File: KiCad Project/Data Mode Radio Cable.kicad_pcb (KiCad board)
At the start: 2 copper layers, 40 x 37 mm, 15 parts, among them J1 TRRS, J2 2.5mm, J3 3.5mm, J4 RS232, SW1 PTT_LOCK, T1 600R, U1 PC817

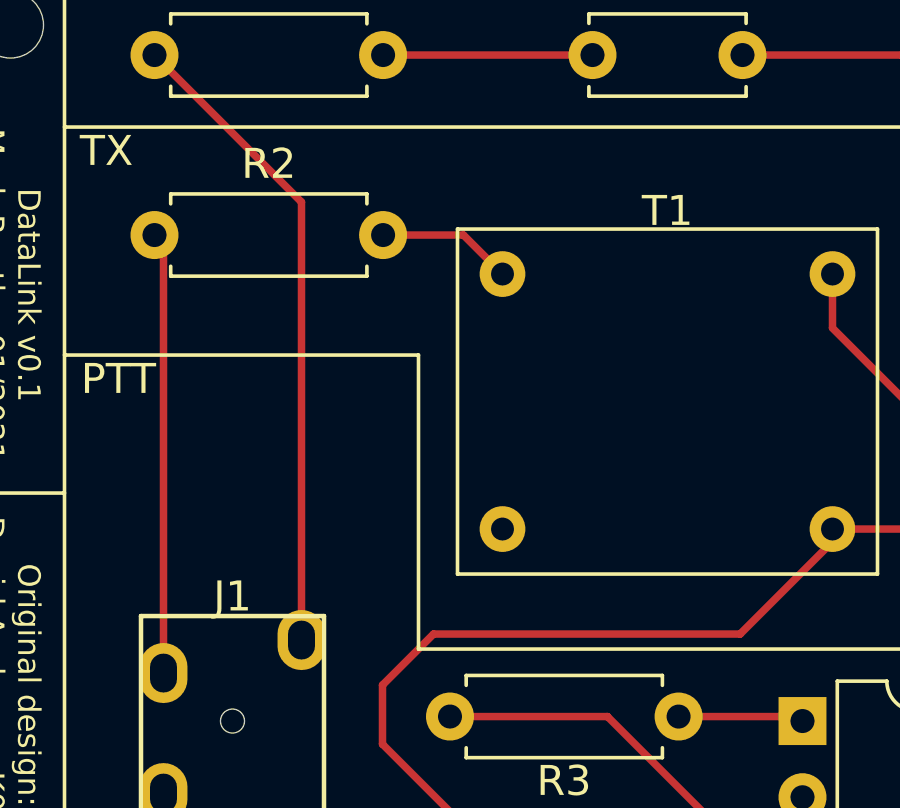
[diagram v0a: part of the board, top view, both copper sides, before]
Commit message: Add files via upload
Replaced project files with ones pointing to new per-project footprints
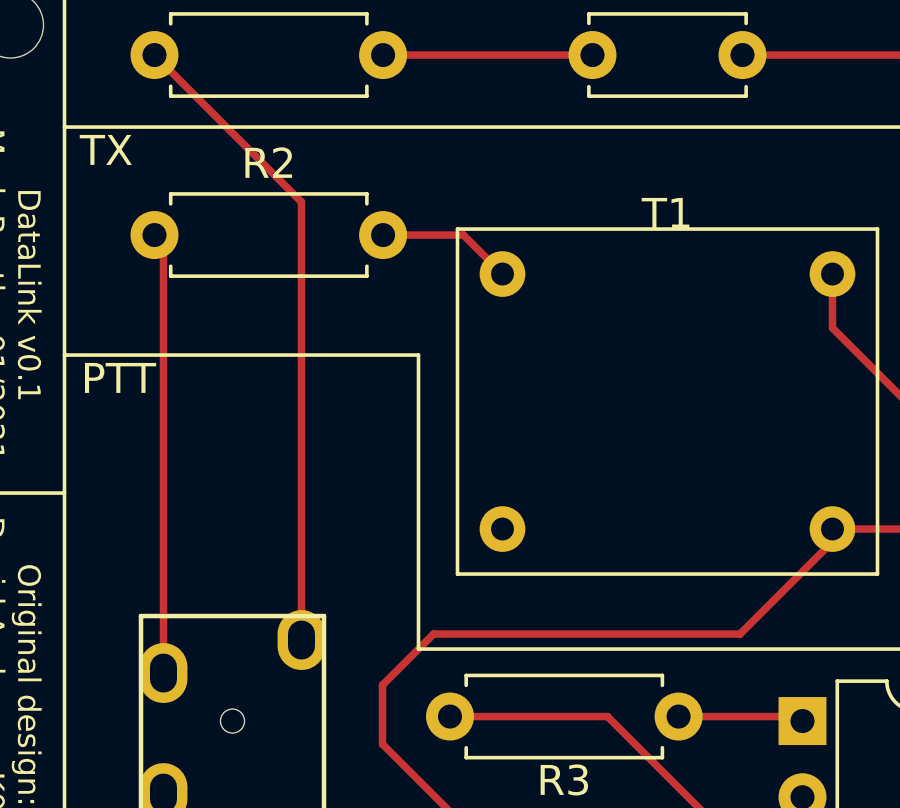
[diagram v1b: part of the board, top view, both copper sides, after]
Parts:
- J1: footprint Keebio-Parts:TRRS-PJ-320A -> Library:TRRS-PJ-320A
- SW1: footprint Custom_Footprints:SPDT_Right_Angled_Switch -> Library:SPDT_Right_Angled_Switch
- T1: footprint Custom_Footprints:1-1_Audio_Transformer_600_ohm -> Library:1-1_Audio_Transformer_600_ohm
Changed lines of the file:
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@@
     (pad "" np_thru_hole circle locked (at 0 0) (size 2.2 2.2) (drill 2.2) (layers *.Cu *.Mask))
   )
-  (footprint "Keebio-Parts:TRRS-PJ-320A" (layer "F.Cu")
+  (footprint "Library:TRRS-PJ-320A" (layer "F.Cu")
     (at 58.6 79 180)
     (property "Sheetfile" "Data Mode Radio Cable.kicad_sch")
     (property "Sheetname" "")
     (attr through_hole)
-    (fp_text reference "J1" (at 0 12.75 180) (layer "F.SilkS")
+    (fp_text reference "J1" (at 0 14.2 180) (layer "Dwgs.User")
       (effects (font (size 1 1) (thickness 0.15)))
     )
@@
       (effects (font (size 1 1) (thickness 0.15)))
     )
+    (fp_text user "Tip" (at 0 10 180) (layer "F.Fab")
+      (effects (font (size 0.7 0.7) (thickness 0.1)))
+    )
     (fp_text user "Ring2" (at 0 3.25 180) (layer "F.Fab")
       (effects (font (size 0.7 0.7) (thickness 0.1)))
     )
-    (fp_text user "Tip" (at 0 10 180) (layer "F.Fab")
+    (fp_text user "Sleeve" (at 0.25 11.4 180) (layer "F.Fab")
       (effects (font (size 0.7 0.7) (thickness 0.1)))
     )
@@
       (effects (font (size 0.7 0.7) (thickness 0.1)))
     )
-    (fp_text user "Sleeve" (at 0.25 11.4 180) (layer "F.Fab")
-      (effects (font (size 0.7 0.7) (thickness 0.1)))
-    )
+    (fp_line (start -2.8 0) (end -2.8 -2) (layer "F.SilkS") (width 0.15))
+    (fp_line (start 3.05 12.1) (end -3.05 12.1) (layer "F.SilkS") (width 0.15))
+    (fp_line (start 3.05 0) (end 3.05 12.1) (layer "F.SilkS") (width 0.15))
+    (fp_line (start 3.05 0) (end -3.05 0) (layer "F.SilkS") (width 0.15))
+    (fp_line (start 2.8 -2) (end -2.8 -2) (layer "F.SilkS") (width 0.15))
+    (fp_line (start 2.8 0) (end 2.8 -2) (layer "F.SilkS") (width 0.15))
     (fp_line (start -3.05 0) (end -3.05 12.1) (layer "F.SilkS") (width 0.15))
-    (fp_line (start 2.8 -2) (end -2.8 -2) (layer "F.SilkS") (width 0.15))
-    (fp_line (start 3.05 0) (end -3.05 0) (layer "F.SilkS") (width 0.15))
-    (fp_line (start 3.05 12.1) (end -3.05 12.1) (layer "F.SilkS") (width 0.15))
-    (fp_line (start -2.8 0) (end -2.8 -2) (layer "F.SilkS") (width 0.15))
-    (fp_line (start 2.8 0) (end 2.8 -2) (layer "F.SilkS") (width 0.15))
-    (fp_line (start 3.05 0) (end 3.05 12.1) (layer "F.SilkS") (width 0.15))
-    (pad "" np_thru_hole circle locked (at 0 8.6 180) (size 0.8 0.8) (drill 0.8) (layers *.Cu *.Mask))
-    (pad "" np_thru_hole circle locked (at 0 1.6 180) (size 0.8 0.8) (drill 0.8) (layers *.Cu *.Mask))
-    (pad "R1" thru_hole oval locked (at 2.3 6.2 180) (size 1.6 2) (drill oval 0.9 1.3) (layers *.Cu *.Mask)
+    (pad "" np_thru_hole circle (at 0 8.6 180) (size 0.8 0.8) (drill 0.8) (layers *.Cu *.Mask))
+    (pad "" np_thru_hole circle (at 0 1.6 180) (size 0.8 0.8) (drill 0.8) (layers *.Cu *.Mask))
+    (pad "R1" thru_hole oval (at 2.3 6.2 180) (size 1.6 2) (drill oval 0.9 1.3) (layers *.Cu *.Mask)
       (net 12 "unconnected-(J1-PadR1)") (pintype "passive+no_connect"))
-    (pad "R2" thru_hole oval locked (at 2.3 3.2 180) (size 1.6 2) (drill oval 0.9 1.3) (layers *.Cu *.Mask)
+    (pad "R2" thru_hole oval (at 2.3 3.2 180) (size 1.6 2) (drill oval 0.9 1.3) (layers *.Cu *.Mask)
       (net 3 "GND") (pintype "passive"))
-    (pad "S" thru_hole oval locked (at -2.3 11.3 180) (size 1.6 2) (drill oval 0.9 1.3) (layers *.Cu *.Mask)
+    (pad "S" thru_hole oval (at -2.3 11.3 180) (size 1.6 2) (drill oval 0.9 1.3) (layers *.Cu *.Mask)
       (net 6 "Net-(J1-PadS)") (pintype "passive"))
-    (pad "T" thru_hole oval locked (at 2.3 10.2 180) (size 1.6 2) (drill oval 0.9 1.3) (layers *.Cu *.Mask)
+    (pad "T" thru_hole oval (at 2.3 10.2 180) (size 1.6 2) (drill oval 0.9 1.3) (layers *.Cu *.Mask)
       (net 7 "Net-(J1-PadT)") (pintype "passive"))
-    (model "${KISYS3DMOD}/Custom.3dshapes/PJ-320A.step"
+    (model "${KIPRJMOD}/3D Models/PJ-320A.step"
       (offset (xyz 0 -1 0))
       (scale (xyz 1 1 1))
@@
     )
   )
-  (footprint "Custom_Footprints:1-1_Audio_Transformer_600_ohm" (layer "F.Cu")
+  (footprint "Library:1-1_Audio_Transformer_600_ohm" (layer "F.Cu")
     (at 73.1 67)
     (property "Sheetfile" "Data Mode Radio Cable.kicad_sch")
     (property "Sheetname" "")
     (attr through_hole)
-    (fp_text reference "T1" (at 0 -13.6) (layer "F.SilkS")
+    (fp_text reference "T1" (at 0 -13.5) (layer "F.SilkS")
       (effects (font (size 1 1) (thickness 0.15)))
     )
@@
       (effects (font (size 1 1) (thickness 0.15)))
     )
+    (fp_line (start -7 -1.5) (end 7 -1.5) (layer "F.SilkS") (width 0.12))
+    (fp_line (start 7 -13) (end -7 -13) (layer "F.SilkS") (width 0.12))
     (fp_line (start -7 -13) (end -7 -1.5) (layer "F.SilkS") (width 0.12))
     (fp_line (start 7 -1.5) (end 7 -13) (layer "F.SilkS") (width 0.12))
-    (fp_line (start 7 -13) (end -7 -13) (layer "F.SilkS") (width 0.12))
-    (fp_line (start -7 -1.5) (end 7 -1.5) (layer "F.SilkS") (width 0.12))
-    (pad "1" thru_hole circle locked (at -5.5 -11.5) (size 1.524 1.524) (drill 0.762) (layers *.Cu *.Mask)
+    (pad "1" thru_hole circle (at -5.5 -11.5) (size 1.524 1.524) (drill 0.762) (layers *.Cu *.Mask)
       (net 8 "Net-(R2-Pad2)") (pinfunction "AA") (pintype "passive"))
-    (pad "2" thru_hole circle locked (at -5.5 -3) (size 1.524 1.524) (drill 0.762) (layers *.Cu *.Mask)
+    (pad "2" thru_hole circle (at -5.5 -3) (size 1.524 1.524) (drill 0.762) (layers *.Cu *.Mask)
       (net 3 "GND") (pinfunction "AB") (pintype "passive"))
-    (pad "3" thru_hole circle locked (at 5.5 -3) (size 1.524 1.524) (drill 0.762) (layers *.Cu *.Mask)
+    (pad "3" thru_hole circle (at 5.5 -3) (size 1.524 1.524) (drill 0.762) (layers *.Cu *.Mask)
       (net 5 "Net-(J3-Pad2)") (pinfunction "SA") (pintype "passive"))
-    (pad "4" thru_hole circle locked (at 5.5 -11.5) (size 1.524 1.524) (drill 0.762) (layers *.Cu *.Mask)
+    (pad "4" thru_hole circle (at 5.5 -11.5) (size 1.524 1.524) (drill 0.762) (layers *.Cu *.Mask)
       (net 4 "Net-(J3-Pad1)") (pinfunction "SB") (pintype "passive"))
-    (model "${KISYS3DMOD}/Custom.3dshapes/4 pin audio transformer.wrl"
+    (model "${KIPRJMOD}/3D Models/4 pin audio transformer.wrl"
       (offset (xyz 0 0 0))
       (scale (xyz 1 1 1))
@@
     )
   )
-  (footprint "Custom_Footprints:SPDT_Right_Angled_Switch" (layer "F.Cu")
+  (footprint "Library:SPDT_Right_Angled_Switch" (layer "F.Cu")
     (at 68.55 77.9 180)
     (property "Sheetfile" "Data Mode Radio Cable.kicad_sch")
     (property "Sheetname" "")
     (attr through_hole)
-    (fp_text reference "SW1" (at -0.254 0.246) (layer "F.SilkS")
+    (fp_text reference "SW1" (at -0.254 0.246 180) (layer "F.SilkS")
       (effects (font (size 1 1) (thickness 0.15)))
     )
-    (fp_text value "PTT_LOCK" (at 0 3.81) (layer "F.Fab")
+    (fp_text value "PTT_LOCK" (at 0 3.81 180) (layer "F.Fab")
       (effects (font (size 1 1) (thickness 0.15)))
     )
     (fp_line (start 4.826 2.794) (end 4.826 -2.794) (layer "F.SilkS") (width 0.12))
-    (fp_line (start -4.826 2.794) (end 4.826 2.794) (layer "F.SilkS") (width 0.12))
-    (fp_line (start -4.826 -2.794) (end -4.826 2.794) (layer "F.SilkS") (width 0.12))
     (fp_line (start 4.826 -2.794) (end -4.826 -2.794) (layer "F.SilkS") (width 0.12))
     (fp_line (start -4.826 0.762) (end 4.826 0.762) (layer "F.SilkS") (width 0.12))
+    (fp_line (start -4.826 -2.794) (end -4.826 2.794) (layer "F.SilkS") (width 0.12))
+    (fp_line (start -4.826 2.794) (end 4.826 2.794) (layer "F.SilkS") (width 0.12))
+    (fp_line (start 5.08 3.048) (end -5.08 3.048) (layer "F.CrtYd") (width 0.05))
+    (fp_line (start 5.08 -3.048) (end 5.08 3.048) (layer "F.CrtYd") (width 0.05))
     (fp_line (start -5.08 -3.048) (end 5.08 -3.048) (layer "F.CrtYd") (width 0.05))
-    (fp_line (start 5.08 3.048) (end -5.08 3.048) (layer "F.CrtYd") (width 0.05))
     (fp_line (start -5.08 3.048) (end -5.08 -3.048) (layer "F.CrtYd") (width 0.05))
-    (fp_line (start 5.08 -3.048) (end 5.08 3.048) (layer "F.CrtYd") (width 0.05))
-    (pad "1" thru_hole circle locked (at -3 1.778 180) (size 1.524 1.524) (drill oval 1 0.462) (layers *.Cu *.Mask)
+    (pad "1" thru_hole circle (at -3 1.778 180) (size 1.524 1.524) (drill oval 1 0.462) (layers *.Cu *.Mask)
       (net 3 "GND") (pinfunction "A") (pintype "passive"))
-    (pad "2" thru_hole circle locked (at 0 1.778 180) (size 1.524 1.524) (drill oval 1 0.462) (layers *.Cu *.Mask)
+    (pad "2" thru_hole circle (at 0 1.778 180) (size 1.524 1.524) (drill oval 1 0.462) (layers *.Cu *.Mask)
       (net 5 "Net-(J3-Pad2)") (pinfunction "B") (pintype "passive"))
-    (pad "3" thru_hole circle locked (at 3 1.778 180) (size 1.524 1.524) (drill oval 1 0.462) (layers *.Cu *.Mask)
+    (pad "3" thru_hole circle (at 3 1.778 180) (size 1.524 1.524) (drill oval 1 0.462) (layers *.Cu *.Mask)
       (net 13 "unconnected-(SW1-Pad3)") (pinfunction "C") (pintype "passive+no_connect"))
-    (model "${KISYS3DMOD}/Custom.3dshapes/SPDT Switch.wrl"
+    (model "${KIPRJMOD}/3D Models/SPDT Switch.wrl"
       (offset (xyz 0 0 0))
       (scale (xyz 1 1 1))
